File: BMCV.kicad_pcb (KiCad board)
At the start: 4 copper layers, 80 x 108 mm, 351 parts, among them J1 AudioJack2_SwitchT, J10 AudioJack2_SwitchT, J11 AudioJack2_SwitchT, J12 AudioJack2_SwitchT, J13 DebugPins, J14 USB_C_Receptacle_USB2.0_14P, J16 Conn_02x08_Eurorack, J2 AudioJack2_SwitchT, J3 AudioJack2_SwitchT, J4 AudioJack2_SwitchT, J5 AudioJack2_SwitchT, J6 AudioJack2_SwitchT, J7 AudioJack2_SwitchT, J8 AudioJack2_SwitchT, J9 AudioJack2_SwitchT, SW1 TC002-N11AS2XT-RGB, SW10 TC002-N11AS2XT-RGB, SW11 TC002-N11AS2XT-RGB, SW12 TC002-N11AS2XT-RGB, SW13 TC002-N11AS2XT-RGB, SW14 Reset, SW15 Boot, SW2 TC002-N11AS2XT-RGB, SW3 TC002-N11AS2XT-RGB, SW4 TC002-N11AS2XT-RGB, SW5 TC002-N11AS2XT-RGB, SW6 TC002-N11AS2XT-RGB, SW7 TC002-N11AS2XT-RGB, SW8 TC002-N11AS2XT-RGB, SW9 TC002-N11AS2XT-RGB, U1 PEL12T-4225S-S1024, U10 WS2811F, U11 WS2811F, U12 WS2811F, U13 WS2811F, U14 WS2811F, U15 WS2811F, U16 WS2811F, U17 WS2811F, U18 WS2811F, U19 WS2811F, U2 PEL12T-4225S-S1024, U20 WS2811F, U21 WS2811F, U22 WS2811F, U23 WS2811F, U24 WS2811F, U25 WS2811F, U26 WS2811F, U27 WS2811F, U28 WS2811F, U29 WS2811F, U3 PEL12T-4225S-S1024, U30 MCP23S17_SS, U31 MCP23S17_SS, U32 TXS0108EPW, U33 AD7367-5, U34 AD5754R, U35 AD5754R, U36 STM32G474CETx, U37 MB85RS64PNF-G-JNERE1, U38 OPA4171, U39 OPA4171, U4 PEL12T-4225S-S1024, U40 OPA4171, U41 TLV76733, U5 PEL12T-4225S-S1024, U6 PEL12T-4225S-S1024, U7 PEL12T-4225S-S1024, U8 PEL12T-4225S-S1024, U9 WS2811F, Y1 38.4MHz 10pF

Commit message: pcb changes
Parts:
- added C100: 1nF, Capacitor_SMD:C_0402_1005Metric, B.Cu at (77.5, 38.8)
- added C101: 1nF, Capacitor_SMD:C_0402_1005Metric, B.Cu at (71.2, 50.6)
- added C102: 1nF, Capacitor_SMD:C_0402_1005Metric, B.Cu at (68.8, 50.6)
- added C103: 1nF, Capacitor_SMD:C_0402_1005Metric, B.Cu at (62.6, 38.8)
- R10, R11, R12, R13, R14, R15, R16, R21, R22, R23, R24, R5: value 10M -> 1M
- moved R95 1.99 mm to (83.7, 59.1), turned to 180 degrees
- moved R10 0.59 mm to (73.4, 51.4)
- moved R134 0.47 mm to (81.5, 59.1)
- moved R11 0.38 mm to (66.5, 51.5)
- moved C75 0.16 mm to (88.7, 58.5)
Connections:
- U35 pad 16: ADC_DAC_SDO -> DAC_2_SDO
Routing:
- net ADC_DAC_SDO: track 80.7 -> 68.6 mm
- net Net-(RV3-A2): track 14.5 -> 19.2 mm
- net Net-(RV2-A2): track 14.2 -> 18.7 mm
- net GND: track 213.0 -> 216.8 mm, vias 637 -> 636
- net Net-(RV1-A2): track 13.7 -> 15.3 mm
- net Net-(U3-SW): track 5.10 -> 3.57 mm
- net Net-(RV4-A2): track 13.6 -> 15.0 mm
- net ENC_2_SW: track 29.9 -> 29.4 mm

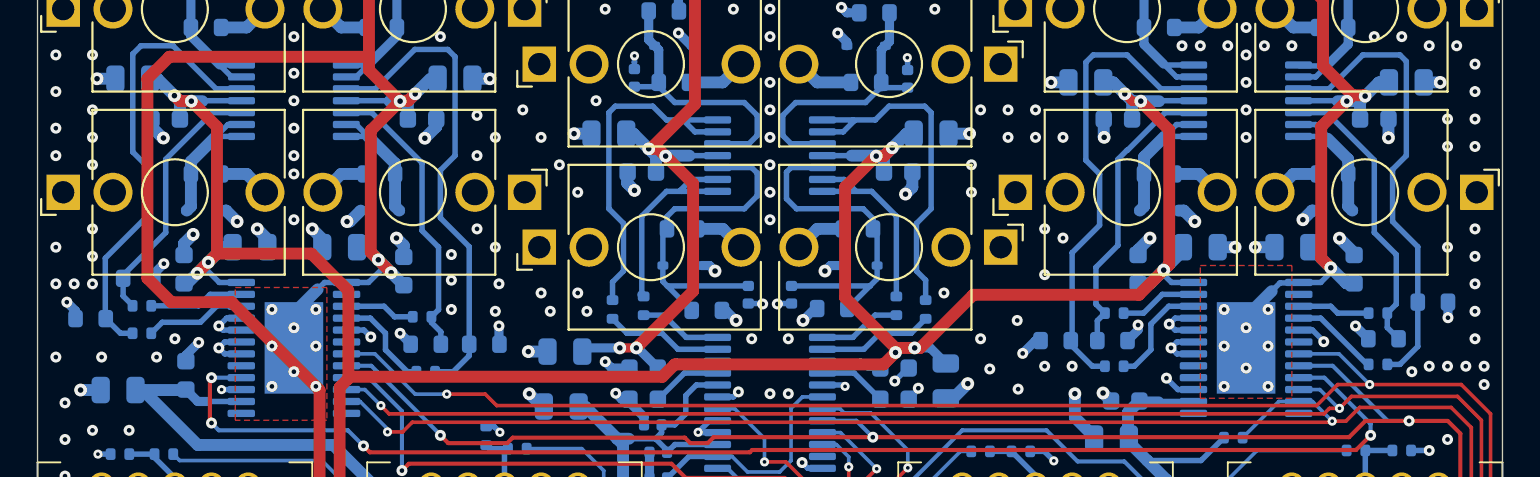
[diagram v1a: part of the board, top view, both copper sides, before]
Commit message: RC filters on DAC output
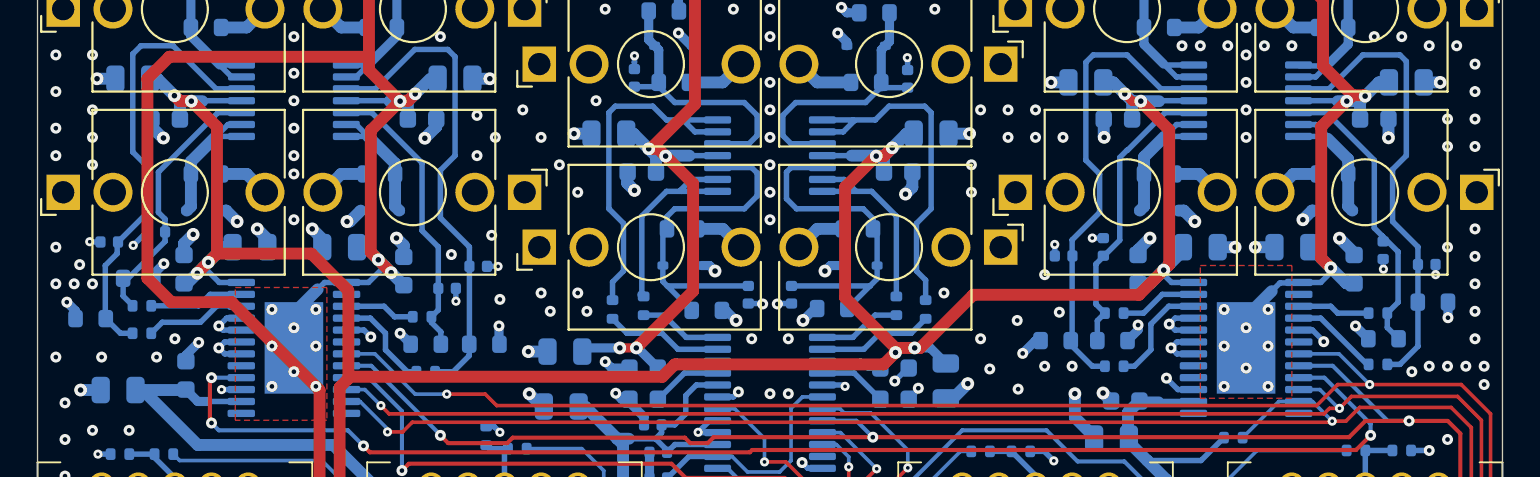
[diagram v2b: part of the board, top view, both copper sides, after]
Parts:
- added C104: 220n, Capacitor_SMD:C_0402_1005Metric, B.Cu at (52.4, 50.2)
- added C105: 220n, Capacitor_SMD:C_0402_1005Metric, B.Cu at (54.1, 49.0)
- added C106: 220n, Capacitor_SMD:C_0402_1005Metric, B.Cu at (33.9, 47.7)
- added C107: 220n, Capacitor_SMD:C_0402_1005Metric, B.Cu at (36.5, 47.2)
- added C108: 220n, Capacitor_SMD:C_0402_1005Metric, B.Cu at (88.2, 48.0)
- added C109: 220n, Capacitor_SMD:C_0402_1005Metric, B.Cu at (86.0, 48.5)
- added C110: 220n, Capacitor_SMD:C_0402_1005Metric, B.Cu at (105.9, 48.9)
- added C111: 220n, Capacitor_SMD:C_0402_1005Metric, B.Cu at (103.5, 48.2)
- C100, C101, C102, C103: value 1nF -> 1n
- C85, C86: value 680nF -> 680n
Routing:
- net GND: track 216.8 -> 222.1 mm, vias 636 -> 638

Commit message: pcb routing
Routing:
- net Net-(U24-VDD): track 6.07 -> 1.93 mm
- net Net-(U25-VDD): track 6.07 -> 1.93 mm
- net Net-(U29-VDD): track 6.07 -> 1.93 mm
- net Net-(U28-VDD): track 6.07 -> 1.93 mm
- net Net-(U27-VDD): track 6.07 -> 1.93 mm
- net Net-(U26-VDD): track 6.07 -> 1.93 mm
- net Net-(U23-VDD): track 6.07 -> 2.03 mm
- net Net-(U19-VDD): track 5.91 -> 1.91 mm
- net Net-(U18-VDD): track 5.91 -> 1.91 mm
- net Net-(U17-VDD): track 5.91 -> 1.91 mm
- net Net-(U20-VDD): track 5.91 -> 1.91 mm
- net Net-(U21-VDD): track 5.80 -> 1.83 mm
- net Net-(U22-VDD): track 5.91 -> 1.94 mm
